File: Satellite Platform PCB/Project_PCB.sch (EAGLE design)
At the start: 15 parts, among them IC1 A4990KLPTR-T, IC2 A4990KLPTR-T, IC3 7805T

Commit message: Finished wiring schematic
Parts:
- removed IC2: A4990KLPTR-T, A4990KLPTR-T:A4990KLPTR-T
- removed X9: (no value), ME507:SCREWTERM_4P_254
- added C1, C2, C3, C4, C5, C6, C7, C8: (no value), rcl:C-USC0805
- added IC4: A4990KLPTR-T, A4990KLPTR-T:A4990KLPTR-T
- added R1, R2, R3, R4: (no value), rcl:R-US_R0805
- added X1: (no value), ME507:SCREWTERM_4P_254
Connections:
- removed net N$3: 3S_BATTERY.1
- new net N$12: C1.1, IC1.CP1
- new net N$13: C1.2, IC1.CP2
- new net N$14: IC1.OUT4, X10-4.1
- new net N$15: IC1.OUT1, X10-1.1
- new net N$16: IC1.OUT2, X10-2.1
- new net N$17: IC1.OUT3, X10-3.1
- new net N$18: C4.2, IC1.VCP
- new net N$19: IC1.SENS34, R1.2
- new net N$20: IC1.SENS12, R3.2
- new net N$21: 3S_BATTERY.1, C3.1, C4.1, C7.1, C8.1, IC1.VBB_1, IC4.VBB_1
- new net N$22: C2.2, IC1.VREG
- new net N$23: IC1.IN1, U$1.ADC11/GPIO0
- new net N$24: IC1.IN2, U$1.ADC12/GPIO2
- new net N$25: IC1.INH, U$1.ADC13/GPIO15
- new net N$26: IC1.IN4, U$1.ADC4/GPIO32
- new net N$27: IC1.IN3, U$1.ADC5/GPIO33
- new net N$28: C5.1, IC4.CP1
- new net N$29: C5.2, IC4.CP2
- new net N$30: IC4.OUT4, X1-4.1
- new net N$31: IC4.OUT1, X1-1.1
- new net N$32: IC4.OUT2, X1-2.1
- new net N$33: IC4.OUT3, X1-3.1
- new net N$34: IC4.SENS34, R2.2
- new net N$35: IC4.SENS12, R4.2
- new net N$37: C8.2, IC4.VCP
- new net N$38: C6.2, IC4.VREG
- new net N$39: IC4.IN1, U$1.ADC18/GPIO25
- new net N$40: IC4.IN2, U$1.ADC19/GPIO26
- new net N$41: IC4.INH, U$1.ADC17/GPIO27
- new net N$42: IC4.IN4, U$1.ADC16/GPIO14
- new net N$43: IC4.IN3, U$1.ADC15/GPIO12
- net GND: now also C2.1, C3.2, C6.1, C7.2, IC1.GND, IC4.GND, R1.1, R2.1, R3.1, R4.1
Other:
- moved on the sheet: IC1, X10-1, X10-2, X10-3, X10-4

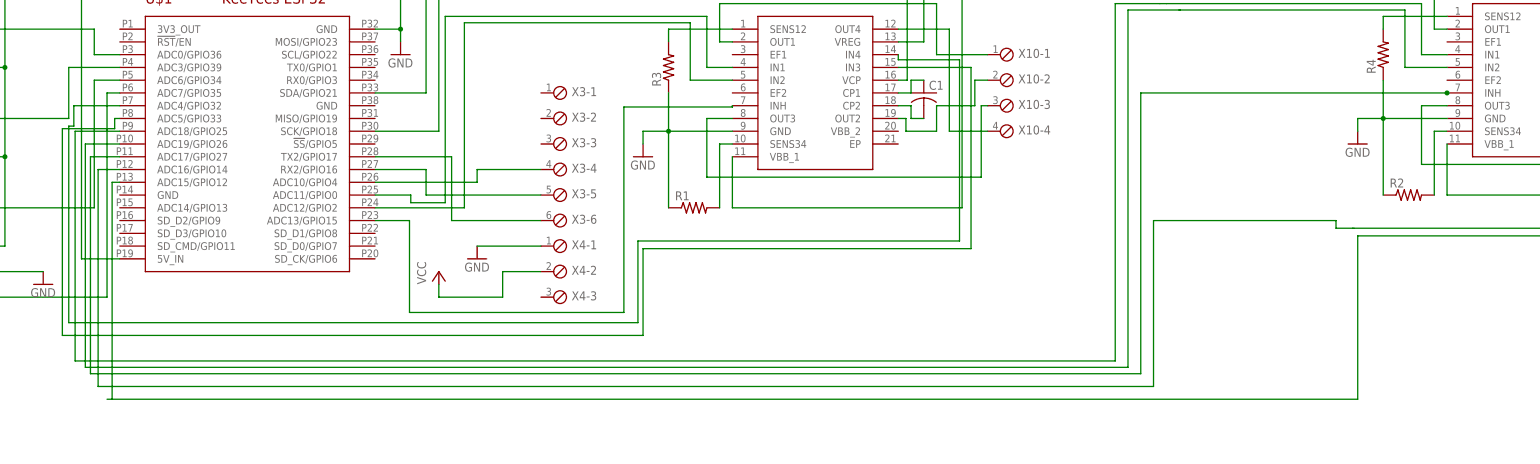
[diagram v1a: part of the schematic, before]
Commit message: Attached enable pins together
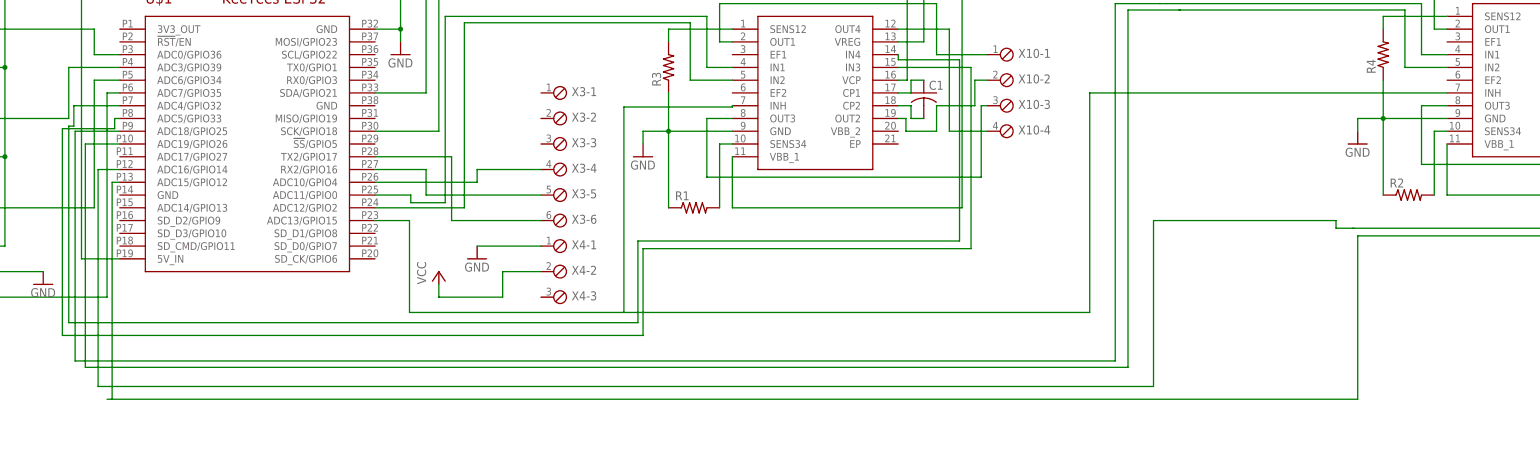
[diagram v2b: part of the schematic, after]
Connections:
- removed net N$41: IC4.INH, U$1.ADC17/GPIO27
- net N$25: now also IC4.INH
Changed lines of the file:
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@@
 <wire x1="73.66" y1="60.706" x2="52.07" y2="60.706" width="0.1524" layer="91"/>
 <wire x1="52.07" y1="60.706" x2="52.07" y2="19.812" width="0.1524" layer="91"/>
-<wire x1="52.07" y1="19.812" x2="9.398" y2="19.812" width="0.1524" layer="91"/>
+<wire x1="52.07" y1="19.812" x2="51.562" y2="19.812" width="0.1524" layer="91"/>
+<wire x1="51.562" y1="19.812" x2="9.398" y2="19.812" width="0.1524" layer="91"/>
 <wire x1="9.398" y1="19.812" x2="9.398" y2="38.1" width="0.1524" layer="91"/>
 <pinref part="U$1" gate="G$1" pin="ADC13/GPIO15"/>
 <wire x1="9.398" y1="38.1" x2="2.54" y2="38.1" width="0.1524" layer="91"/>
+<pinref part="IC4" gate="G$1" pin="INH"/>
+<wire x1="215.9" y1="63.5" x2="144.78" y2="63.5" width="0.1524" layer="91"/>
+<wire x1="144.78" y1="63.5" x2="144.78" y2="19.812" width="0.1524" layer="91"/>
+<wire x1="144.78" y1="19.812" x2="52.07" y2="19.812" width="0.1524" layer="91"/>
 </segment>
 </net>
@@
 </segment>
 </net>
-<net name="N$41" class="0">
-<segment>
-<wire x1="215.9" y1="63.5" x2="215.9" y2="63.246" width="0.1524" layer="91"/>
-<pinref part="IC4" gate="G$1" pin="INH"/>
-<pinref part="U$1" gate="G$1" pin="ADC17/GPIO27"/>
-<wire x1="-48.26" y1="50.8" x2="-54.102" y2="50.8" width="0.1524" layer="91"/>
-<wire x1="-54.102" y1="50.8" x2="-54.102" y2="7.62" width="0.1524" layer="91"/>
-<wire x1="-54.102" y1="7.62" x2="154.94" y2="7.62" width="0.1524" layer="91"/>
-<wire x1="154.94" y1="7.62" x2="154.94" y2="63.5" width="0.1524" layer="91"/>
-<wire x1="154.94" y1="63.5" x2="215.9" y2="63.5" width="0.1524" layer="91"/>
-<junction x="215.9" y="63.5"/>
-</segment>
-</net>

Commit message: Added diode
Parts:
- added U$2: MBRM140T3G, MBRM140T3G:MBRM140T3G
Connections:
- new net N$3: 3S_BATTERY.1, U$2.A
- net N$21: now also U$2.C; no longer 3S_BATTERY.1
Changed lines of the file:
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@@
 <part name="FRAME1" library="ME507" deviceset="TITLEBLOCK_TAB_L" device=""/>
 <part name="FRAME2" library="ME507" deviceset="TITLEBLOCK_TAB_L" device=""/>
+<part name="U$2" library="MBRM140T3G" deviceset="MBRM140T3G" device=""/>
 </parts>
 <sheets>
@@
 <attribute name="AUTHOR" x="212.09" y="-49.53" size="2.54" layer="94"/>
 <attribute name="BOARD_NAME" x="201.93" y="-43.18" size="2.54" layer="94"/>
+</instance>
+<instance part="U$2" gate="G$1" x="111.76" y="119.38" smashed="yes" rot="R180">
+<attribute name="NAME" x="114.049909375" y="117.47173125" size="1.781040625" layer="95" rot="R180"/>
+<attribute name="VALUE" x="114.05023125" y="122.81535" size="1.7813" layer="96" rot="R180"/>
 </instance>
 </instances>
@@
 <wire x1="96.52" y1="99.06" x2="96.52" y2="119.38" width="0.1524" layer="91"/>
 <junction x="96.52" y="99.06"/>
-<pinref part="3S_BATTERY" gate="G$1" pin="1"/>
-<wire x1="96.52" y1="119.38" x2="121.92" y2="119.38" width="0.1524" layer="91"/>
 <wire x1="96.52" y1="119.38" x2="96.52" y2="132.08" width="0.1524" layer="91"/>
 <wire x1="96.52" y1="132.08" x2="238.76" y2="132.08" width="0.1524" layer="91"/>
-<junction x="96.52" y="119.38"/>
 <wire x1="215.9" y1="53.34" x2="215.9" y2="43.18" width="0.1524" layer="91"/>
 <wire x1="215.9" y1="43.18" x2="261.62" y2="43.18" width="0.1524" layer="91"/>
@@
 <pinref part="C8" gate="G$1" pin="1"/>
 <wire x1="238.76" y1="132.08" x2="238.76" y2="101.6" width="0.1524" layer="91"/>
+<pinref part="U$2" gate="G$1" pin="C"/>
+<wire x1="106.68" y1="119.38" x2="96.52" y2="119.38" width="0.1524" layer="91"/>
+<junction x="96.52" y="119.38"/>
 </segment>
 </net>
@@
 </segment>
 </net>
+<net name="N$3" class="0">
+<segment>
+<pinref part="3S_BATTERY" gate="G$1" pin="1"/>
+<pinref part="U$2" gate="G$1" pin="A"/>
+<wire x1="121.92" y1="119.38" x2="116.84" y2="119.38" width="0.1524" layer="91"/>
+</segment>
+</net>

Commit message: Added all last names to title block
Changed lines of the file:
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@@
 <schematic xreflabel="%F%N/%S.%C%R" xrefpart="/%S.%C%R">
 <attributes>
-<attribute name="AUTHOR" value="Alexander Dunn"/>
+<attribute name="AUTHOR" value="Dunn, Frabosilio, Lee"/>
 <attribute name="BOARD_NAME" value="Satellite Platform Schematic"/>
 <attribute name="PROJECT_NAME" value="ME 507 Project"/>
@@
 <part name="GND9" library="supply1" library_urn="urn:adsk.eagle:library:371" deviceset="GND" device=""/>
 <part name="GND10" library="supply1" library_urn="urn:adsk.eagle:library:371" deviceset="GND" device=""/>
+<part name="U$2" library="MBRM140T3G" deviceset="MBRM140T3G" device=""/>
 <part name="FRAME1" library="ME507" deviceset="TITLEBLOCK_TAB_L" device=""/>
-<part name="FRAME2" library="ME507" deviceset="TITLEBLOCK_TAB_L" device=""/>
-<part name="U$2" library="MBRM140T3G" deviceset="MBRM140T3G" device=""/>
 </parts>
 <sheets>
@@
 <attribute name="VALUE" x="236.22" y="88.9" size="1.778" layer="96"/>
 </instance>
-<instance part="FRAME1" gate="G$1" x="-109.22" y="-66.04" smashed="yes"/>
-<instance part="FRAME2" gate="G$3" x="-105.41" y="-66.04" smashed="yes"/>
-<instance part="FRAME2" gate="G$2" x="189.23" y="-66.04" smashed="yes">
-<attribute name="LAST_DATE_TIME" x="201.93" y="-54.61" size="2.54" layer="94"/>
-<attribute name="SHEET" x="231.14" y="-59.69" size="2.54" layer="94"/>
-<attribute name="DRAWING_NAME" x="282.575" y="-62.23" size="2.54" layer="94" align="bottom-right"/>
-<attribute name="PROJECT_NAME" x="207.01" y="-35.56" size="2.54" layer="94"/>
-<attribute name="AUTHOR" x="212.09" y="-49.53" size="2.54" layer="94"/>
-<attribute name="BOARD_NAME" x="201.93" y="-43.18" size="2.54" layer="94"/>
-</instance>
 <instance part="U$2" gate="G$1" x="111.76" y="119.38" smashed="yes" rot="R180">
 <attribute name="NAME" x="114.049909375" y="117.47173125" size="1.781040625" layer="95" rot="R180"/>
 <attribute name="VALUE" x="114.05023125" y="122.81535" size="1.7813" layer="96" rot="R180"/>
 </instance>
+<instance part="FRAME1" gate="G$3" x="-96.52" y="-60.96" smashed="yes"/>
+<instance part="FRAME1" gate="G$2" x="198.12" y="-60.96" smashed="yes">
+<attribute name="LAST_DATE_TIME" x="210.82" y="-49.53" size="2.54" layer="94"/>
+<attribute name="SHEET" x="240.03" y="-54.61" size="2.54" layer="94"/>
+<attribute name="DRAWING_NAME" x="291.465" y="-57.15" size="2.54" layer="94" align="bottom-right"/>
+<attribute name="PROJECT_NAME" x="215.9" y="-30.48" size="2.54" layer="94"/>
+<attribute name="AUTHOR" x="220.98" y="-44.45" size="2.54" layer="94"/>
+<attribute name="BOARD_NAME" x="210.82" y="-38.1" size="2.54" layer="94"/>
+</instance>
+<instance part="FRAME1" gate="G$1" x="-101.6" y="-63.5" smashed="yes"/>
 </instances>
 <busses>

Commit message: Added R and C values
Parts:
- C1, C5: value (none) -> 100 nF (50V)
- C2, C6: value (none) -> 470 nF (10V)
- C3, C4, C7, C8: value (none) -> 100 nF (16V)
- R1, R2, R3, R4: value (none) -> 375 mOhm

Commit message: added board
airwires still
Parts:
- renumbered X1 to MOTOR2, X10 to MOTOR1, X2 to IMU, X3 to GPS1, X4 to GPS2, X5 to L1, X6 to L2, X7 to L3, X8 to L4

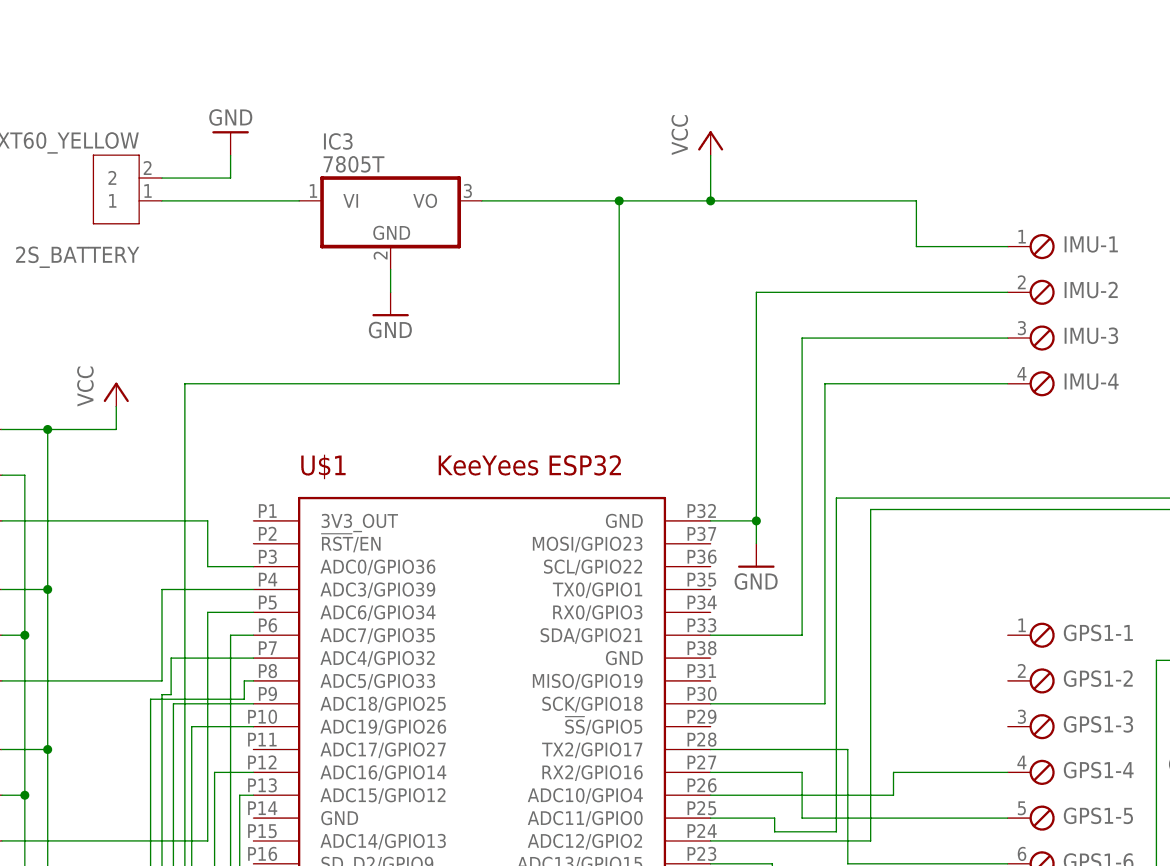
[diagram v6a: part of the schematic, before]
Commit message: rewired
updated based on ridgely's comments
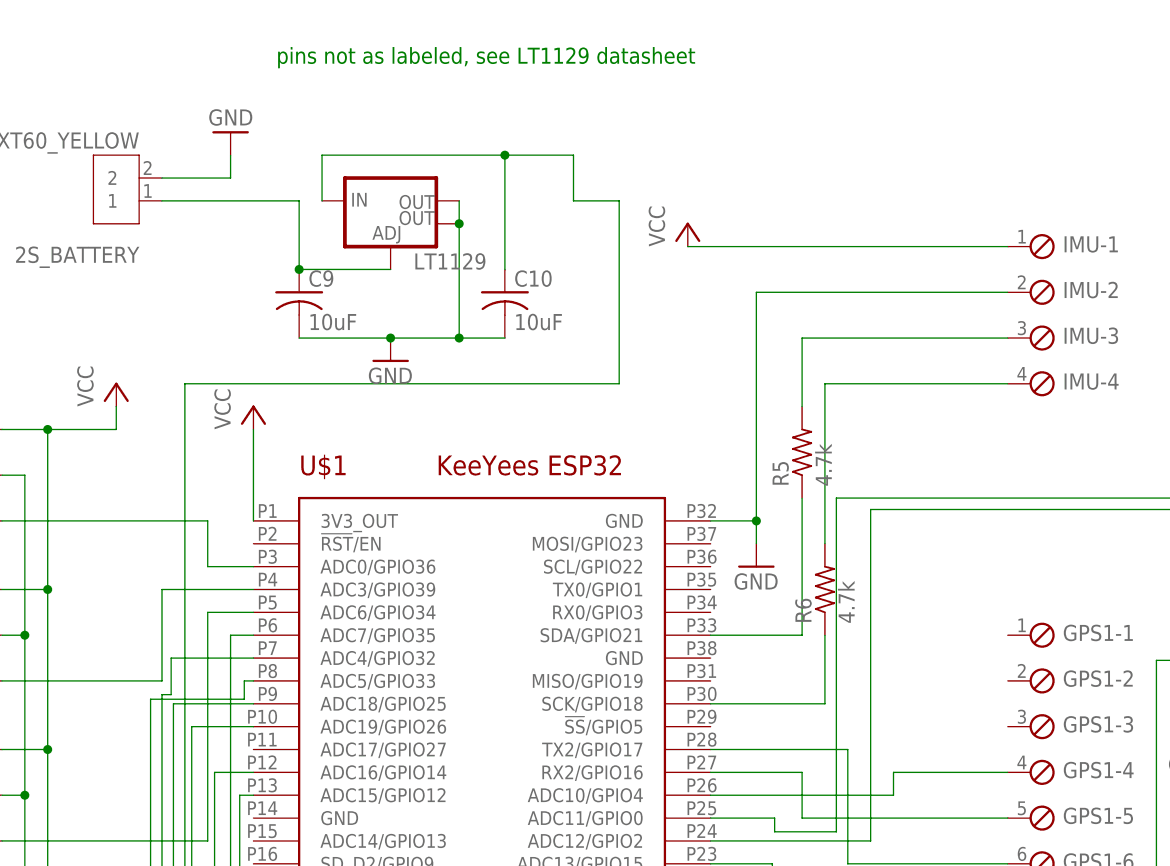
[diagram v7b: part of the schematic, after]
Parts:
- removed IC3: 7805T, adafruit:7805T
- added C10, C9: 10uF, rcl:C-USC0805
- added LT1129: (no value), SparkFun-IC-Power:V_REG_LM1117SOT223
- added R5, R6: 4.7k, rcl:R-US_R0805
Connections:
- new net N$41: R5.1, U$1.SDA/GPIO21
- new net N$44: R6.1, U$1.SCK/GPIO18
- new net N$46: 2S_BATTERY.1, C9.1, LT1129.ADJ
- net GND: now also C10.2, C9.2, LT1129.OUT, LT1129.OUT@1; no longer IC3.GND
- net N$1: now also C10.1, LT1129.IN, U$1.5V_IN; no longer 2S_BATTERY.1, IC3.VI
- net N$10: now also R5.2; no longer U$1.SDA/GPIO21
- net N$11: now also R6.2; no longer U$1.SCK/GPIO18
- net VCC: now also U$1.3V3_OUT; no longer IC3.VO, U$1.5V_IN
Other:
- note added: "pins not as labeled, see LT1129 datasheet"
